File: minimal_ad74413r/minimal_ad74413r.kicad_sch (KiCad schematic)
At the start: 50 parts, among them J1 CLP-102-02-G-D-BE, J2 CLP-102-02-G-D-BE, J3 CLP-104-02-G-D-BE, J4 CLP-104-02-G-D-BE, J5 CLP-102-02-G-D-BE, J6 CLP-102-02-G-D-BE, J7 CLP-114-02-G-D-BE, U1 AD74413RBCPZ

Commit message: Backup
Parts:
- J1, J2, J5, J6: value CLP-102-02-G-D-BE -> FW-02-03-G-D-085-315; footprint connector_footprints:CLP-102-02-G-D-BE -> connector_footprints:FW-02-03-G-D-085-315; symbol UNITED_CONNECTORS_DATA_BASE:J_CLP-102-02-G-D-BE -> UNITED_CONNECTORS_DATA_BASE:J_FW-02-03-G-D-085-315; Contact Plating Tin -> Gold; MPN CLP-102-02-G-D-BE -> FW-02-03-G-D-085-315; Mounting Style Through Hole -> Surface Mount; Series CLP-1xx-02-G-D-BE -> FW-xx-03-G-D-085-315; Symbol Name J_CLP-102-02-G-D-BE -> J_FW-02-03-G-D-085-315; Trustedparts Search https://www.trustedparts.com/en/search/CLP-102-02-G-D-BE -> https://www.trustedparts.com/en/search/FW-02-03-G-D-085-315
- J3, J4: value CLP-104-02-G-D-BE -> FW-04-03-G-D-085-315; footprint connector_footprints:CLP-104-02-G-D-BE -> connector_footprints:FW-04-03-G-D-085-315; symbol UNITED_CONNECTORS_DATA_BASE:J_CLP-104-02-G-D-BE -> UNITED_CONNECTORS_DATA_BASE:J_FW-04-03-G-D-085-315; Contact Plating Tin -> Gold; MPN CLP-104-02-G-D-BE -> FW-04-03-G-D-085-315; Mounting Style Through Hole -> Surface Mount; Series CLP-1xx-02-G-D-BE -> FW-xx-03-G-D-085-315; Symbol Name J_CLP-104-02-G-D-BE -> J_FW-04-03-G-D-085-315; Trustedparts Search https://www.trustedparts.com/en/search/CLP-104-02-G-D-BE -> https://www.trustedparts.com/en/search/FW-04-03-G-D-085-315
- J7: value CLP-114-02-G-D-BE -> FW-14-03-G-D-085-155; footprint connector_footprints:CLP-114-02-G-D-BE -> connector_footprints:FW-14-03-G-D-085-155; symbol UNITED_CONNECTORS_DATA_BASE:J_CLP-114-02-G-D-BE -> UNITED_CONNECTORS_DATA_BASE:J_FW-14-03-G-D-085-155; Contact Plating Tin -> Gold; MPN CLP-114-02-G-D-BE -> FW-14-03-G-D-085-155; Mounting Style Through Hole -> Surface Mount; Series CLP-1xx-02-G-D-BE -> FW-xx-03-G-D-085-155; Symbol Name J_CLP-114-02-G-D-BE -> J_FW-14-03-G-D-085-155; Trustedparts Search https://www.trustedparts.com/en/search/CLP-114-02-G-D-BE -> https://www.trustedparts.com/en/search/FW-14-03-G-D-085-155

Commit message: Update subproject commit and add new configuration and library entries for KiCAD_Symbol_Generator
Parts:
- added MB1, MB2, MB3, MB4, MB5, MB6: mouse-bite-midle-50mil-200mil, mouse_bite_footprints:mouse-bite-midle-50mil-200mil, symbol UNITED_MOUSE_BITES_DATA_BASE:mouse-bite-midle-50mil-200mil
- added MB7: mouse-bite-midle-50mil-200mil, mouse_bite_footprints:mouse-bite-50mil-790mil, symbol UNITED_MOUSE_BITES_DATA_BASE:mouse-bite-50mil-790mil

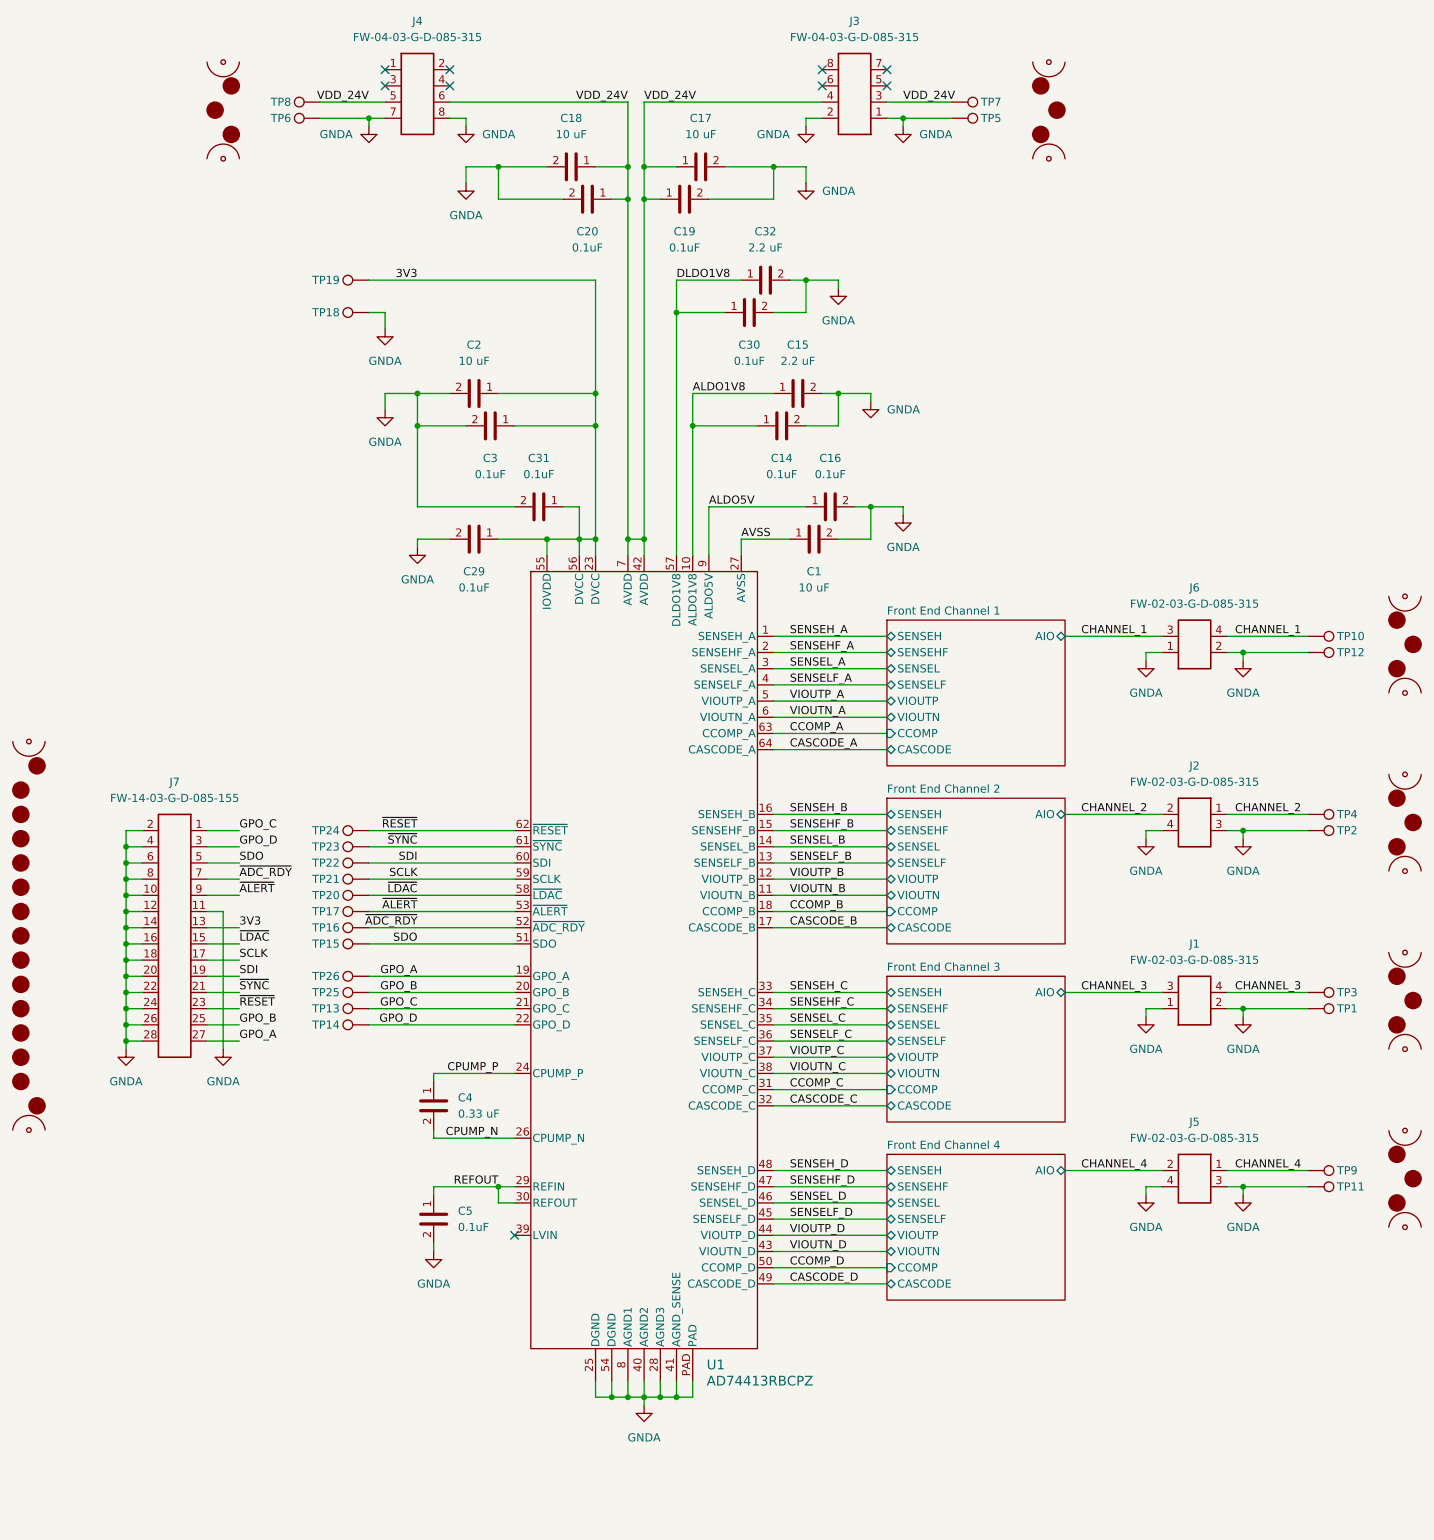
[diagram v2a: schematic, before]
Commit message: Update subproject commit and add new library entries for KiCAD_Symbol_Generator
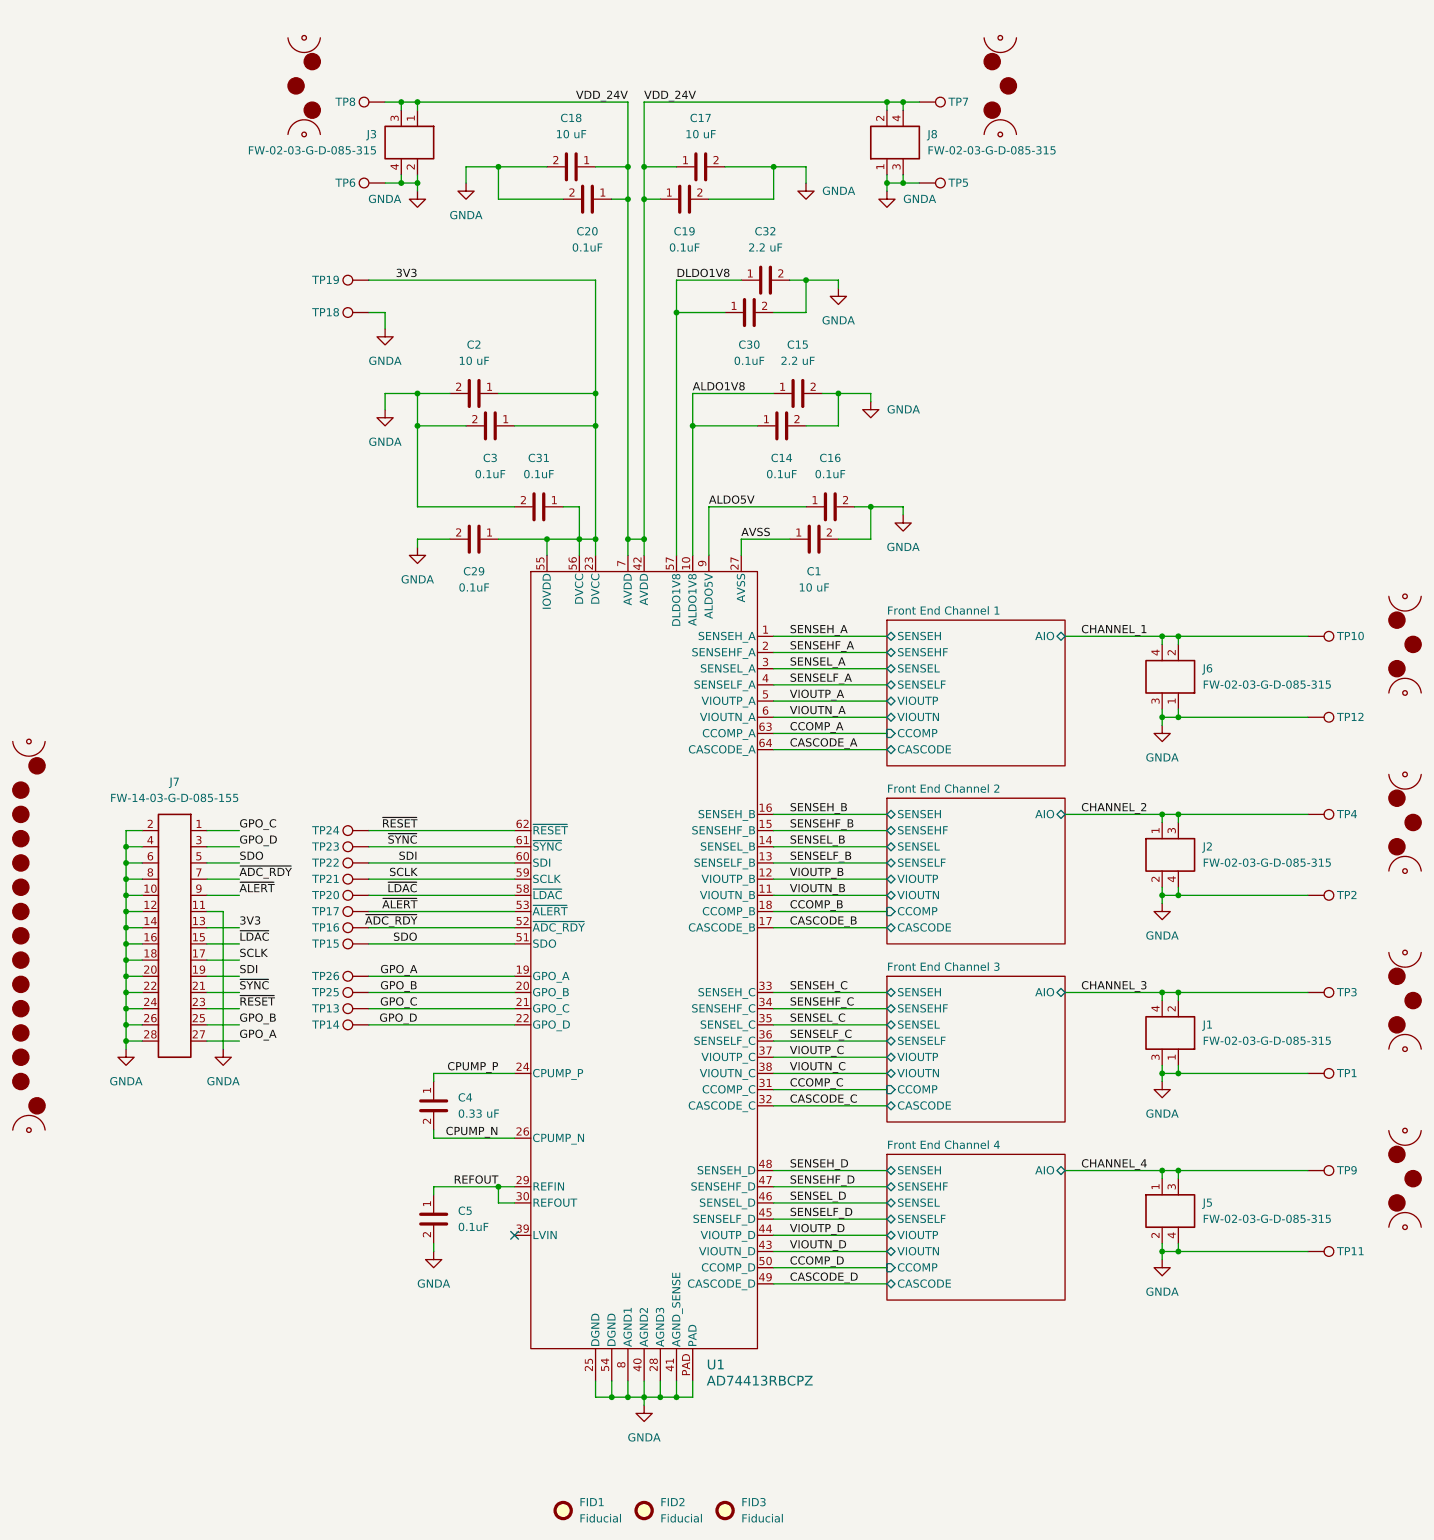
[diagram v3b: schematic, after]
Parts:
- removed J3, J4: FW-04-03-G-D-085-315, connector_footprints:FW-04-03-G-D-085-315, symbol UNITED_CONNECTORS_DATA_BASE:J_FW-04-03-G-D-085-315
- added FID1, FID2, FID3: Fiducial, no_components_footprints:Fiducial_0.5mm_Mask1mm, symbol UNITED_NO_COMPONENTS_DATA_BASE:Fiducial
- added J3, J8: FW-02-03-G-D-085-315, connector_footprints:FW-02-03-G-D-085-315, symbol UNITED_CONNECTORS_DATA_BASE:J_FW-02-03-G-D-085-315
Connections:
- net CHANNEL_1: now also J6.2; no longer J6.3
- net CHANNEL_2: now also J2.3; no longer J2.2
- net CHANNEL_3: now also J1.2; no longer J1.3
- net CHANNEL_4: now also J5.3; no longer J5.2
- net GNDA: now also J1.3, J2.2, J5.2, J6.3, J3.2, J3.4, J8.1, J8.3; no longer J1.2, J2.3, J5.3, J6.2
- net VDD_24V: now also J3.1, J3.3, J8.2, J8.4
- no-connect marks 9 -> 1
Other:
- moved on the sheet: J1, J2, J5, J6, TP1, TP11, TP12, TP2, TP5, TP6, TP7, TP8

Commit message: Update project files and enhance structure
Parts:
- J3, J8: value FW-02-03-G-D-085-315 -> FW-02-03-G-D-085-155; footprint connector_footprints:FW-02-03-G-D-085-315 -> connector_footprints:FW-02-03-G-D-085-155; symbol UNITED_CONNECTORS_DATA_BASE:J_FW-02-03-G-D-085-315 -> UNITED_CONNECTORS_DATA_BASE:J_FW-02-03-G-D-085-155; MPN FW-02-03-G-D-085-315 -> FW-02-03-G-D-085-155; Series FW-xx-03-G-D-085-315 -> FW-xx-03-G-D-085-155; Symbol Name J_FW-02-03-G-D-085-315 -> J_FW-02-03-G-D-085-155; Trustedparts Search https://www.trustedparts.com/en/search/FW-02-03-G-D-085-315 -> https://www.trustedparts.com/en/search/FW-02-03-G-D-085-155
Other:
- moved on the sheet: J3, J8, TP5, TP6, TP7, TP8

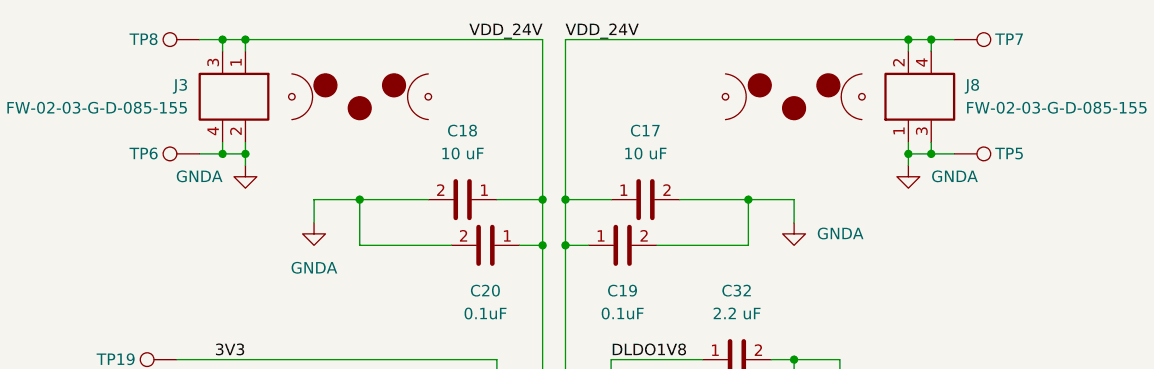
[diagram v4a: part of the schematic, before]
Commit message: Update reference properties in minimal_ad74413r schematic
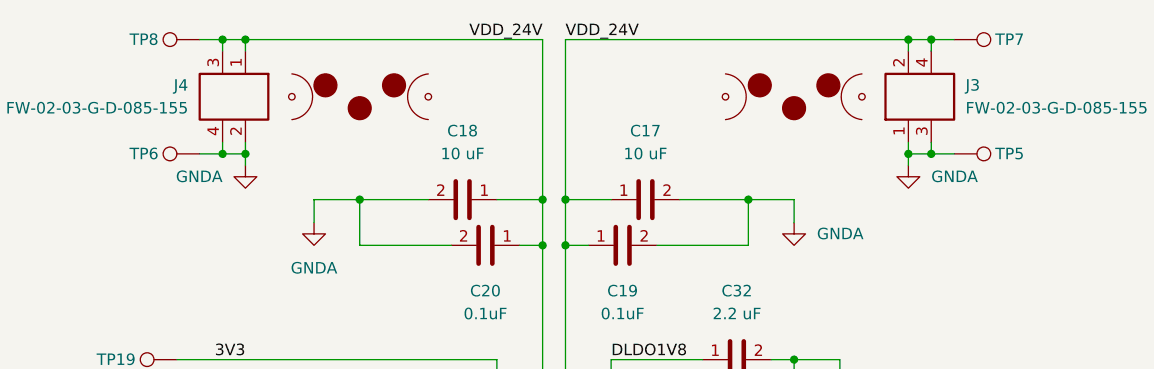
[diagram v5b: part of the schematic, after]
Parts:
- renumbered J8 to J3, J3 to J4, MB4 to MB1, MB3 to MB2, MB5 to MB3, MB2 to MB4, MB6 to MB5, MB1 to MB6
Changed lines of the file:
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@@
 		(dnp no)
 		(fields_autoplaced yes)
-		(property "Reference" "MB2"
+		(property "Reference" "MB4"
 			(at 327.66 146.05 0)
 			(effects
@@
 			(project "minimal_ad74413r"
 				(path "/3d1a8eae-9f4e-4ae3-8a80-a6e3408e9f8d"
-					(reference "MB2")
+					(reference "MB4")
 					(unit 1)
 				)
@@
 		(dnp no)
 		(fields_autoplaced yes)
-		(property "Reference" "J8"
+		(property "Reference" "J3"
 			(at 247.65 30.4799 90)
 			(effects
@@
 			(project "minimal_ad74413r"
 				(path "/3d1a8eae-9f4e-4ae3-8a80-a6e3408e9f8d"
-					(reference "J8")
+					(reference "J3")
 					(unit 1)
 				)
@@
 		(on_board yes)
 		(dnp no)
-		(property "Reference" "MB6"
+		(property "Reference" "MB5"
 			(at 180.34 36.83 0)
 			(effects
@@
 			(project "minimal_ad74413r"
 				(path "/3d1a8eae-9f4e-4ae3-8a80-a6e3408e9f8d"
-					(reference "MB6")
+					(reference "MB5")
 					(unit 1)
 				)
@@
 		(dnp no)
 		(fields_autoplaced yes)
-		(property "Reference" "MB5"
+		(property "Reference" "MB3"
 			(at 228.6 36.83 0)
 			(effects
@@
 			(project "minimal_ad74413r"
 				(path "/3d1a8eae-9f4e-4ae3-8a80-a6e3408e9f8d"
-					(reference "MB5")
+					(reference "MB3")
 					(unit 1)
 				)
@@
 		(dnp no)
 		(fields_autoplaced yes)
-		(property "Reference" "MB3"
+		(property "Reference" "MB2"
 			(at 327.66 173.99 0)
 			(effects
@@
 			(project "minimal_ad74413r"
 				(path "/3d1a8eae-9f4e-4ae3-8a80-a6e3408e9f8d"
-					(reference "MB3")
+					(reference "MB2")
 					(unit 1)
 				)
@@
 		(dnp no)
 		(fields_autoplaced yes)
-		(property "Reference" "MB1"
+		(property "Reference" "MB6"
 			(at 327.66 118.11 0)
 			(effects
@@
 			(project ""
 				(path "/3d1a8eae-9f4e-4ae3-8a80-a6e3408e9f8d"
-					(reference "MB1")
+					(reference "MB6")
 					(unit 1)
 				)
@@
 		(dnp no)
 		(fields_autoplaced yes)
-		(property "Reference" "MB4"
+		(property "Reference" "MB1"
 			(at 327.66 201.93 0)
 			(effects
@@
 			(project "minimal_ad74413r"
 				(path "/3d1a8eae-9f4e-4ae3-8a80-a6e3408e9f8d"
-					(reference "MB4")
+					(reference "MB1")
 					(unit 1)
 				)
@@
 		(dnp no)
 		(fields_autoplaced yes)
-		(property "Reference" "J3"
+		(property "Reference" "J4"
 			(at 161.29 30.4799 90)
 			(effects
@@
 			(project "minimal_ad74413r"
 				(path "/3d1a8eae-9f4e-4ae3-8a80-a6e3408e9f8d"
-					(reference "J3")
+					(reference "J4")
 					(unit 1)
 				)
